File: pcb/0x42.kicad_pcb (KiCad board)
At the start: 2 copper layers, 285 x 95.1 mm, 196 parts, among them J1 USB_C_Receptacle_USB2.0, J2 Conn_01x04, J3 SWD_CN4, K000 1.5U, K001 1U, K002 1U, K003 1U, K004 1U, K005 1U, K006 1U, K007 1U, K008 1U, K009 1U, K010 1U, K011 1U, K012 1U, K013 1.5U, K100 1.5U, K101 1U, K102 1U, K103 1U, K104 1U, K105 1U, K106 1U, K107 1U, K108 1U, K109 1U, K110 1U, K111 1U, K112 1U, K113 1.5U, K200 1.5U, K201 1U, K202 1U, K203 1U, K204 1U, K205 1U, K206 1U, K207 1U, K208 1U, K209 1U, K210 1U, K211 1U, K212 1U, K213 1.5U, K300 1.5U, K301 1U, K302 1U, K303 1U, K304 1U, K305 1U, K306 1U, K307 1U, K308 1U, K309 1U, K310 1U, K311 1U, K312 1U, K313 1.5U, K400 1.5U, K401 1U, K402 1U, K403 1U, K404 1U, K405 1U, K406 1U, K407 1U, K408 1U, K409 1U, K410 1U, K411 1U, K412 1U, K413 1.5U, SW1 Reset, SW2 Boot, U1 STM32F072CBUx, U2 MCP1700-3302E_SOT89, U3 IS31FL3731-QF

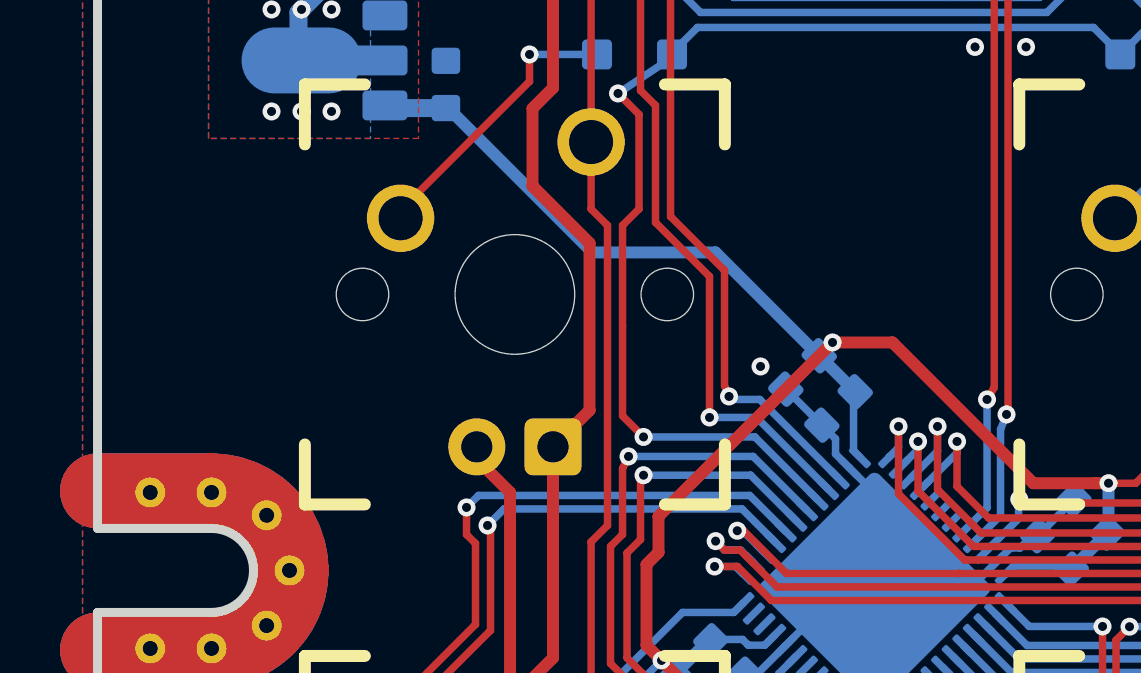
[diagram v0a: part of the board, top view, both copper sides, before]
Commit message: Add RGB output - WiP
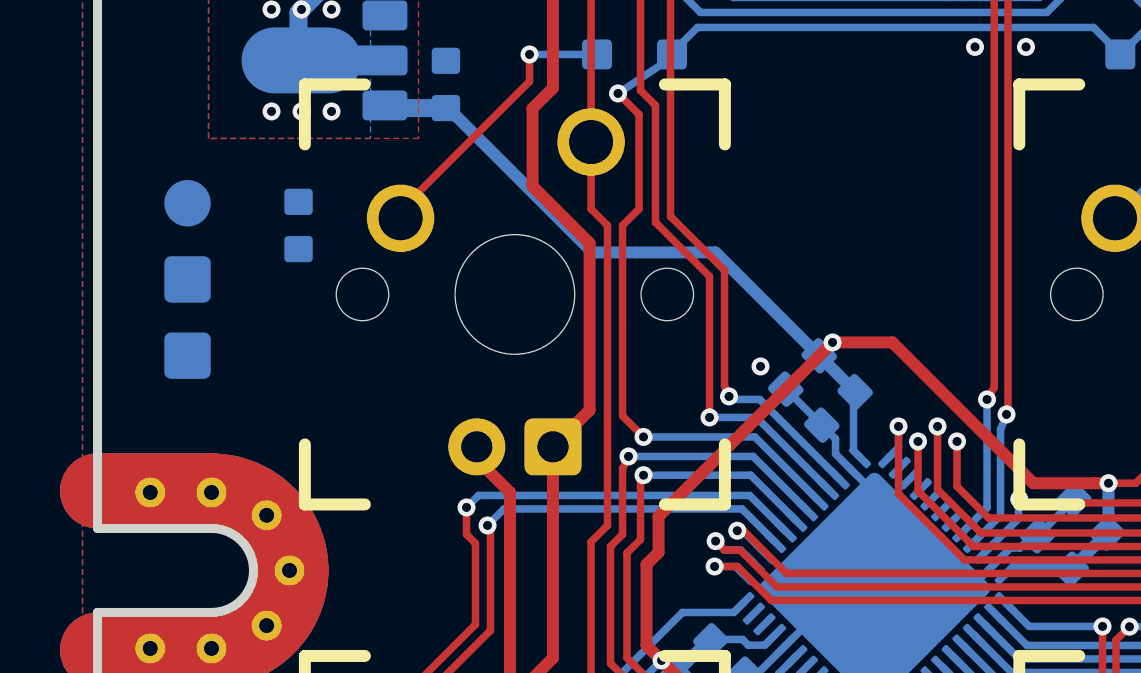
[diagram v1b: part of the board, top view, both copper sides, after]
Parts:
- added J4: Conn_01x03, 0xLib_LED_SMD:RGB_header_VoG_pads, B.Cu at (72.5, 115.5)
- added R12: 4.7k, 0xLib_Passive_SMD:R_0603_1608Metric, B.Cu at (76.2, 113.7)
- C0: value 4n7 -> 4.7n
- C1, C12, C13, Cb1: value 4µ7 -> 4.7µ
- R1, R11, R4, R5, R6, R7: value 10K -> 10k
- R10: value 22K -> 22k
- R8, R9: value 4K7 -> 4.7k
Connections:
- U1 pad 26: Col11 -> Net-(U1-Pad26)
- U1 pad 27: Col12 -> Net-(U1-Pad27)
- U1 pad 28: Col13 -> RGB_DOUT
- U1 pad 29: Net-(U1-Pad29) -> Col11
- U1 pad 30: Net-(U1-Pad30) -> Col12
- U1 pad 31: Net-(U1-Pad31) -> Col13
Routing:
- net Col12: track 309.4 -> 307.3 mm
- net Col13: track 332.1 -> 330.0 mm
- net Col11: track 289.6 -> 288.5 mm
